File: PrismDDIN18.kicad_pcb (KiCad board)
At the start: 2 copper layers, 280 x 60 mm, 93 parts, among them CON1 BARREL_JACK, IC1 LM2596T-5, J1 Conn_01x03, M1 IN-18, M10 IN-18, Q2 2N7000, Q3 2N7000, Q4 2N7000, Q5 2N7000, Q6 IRF540N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

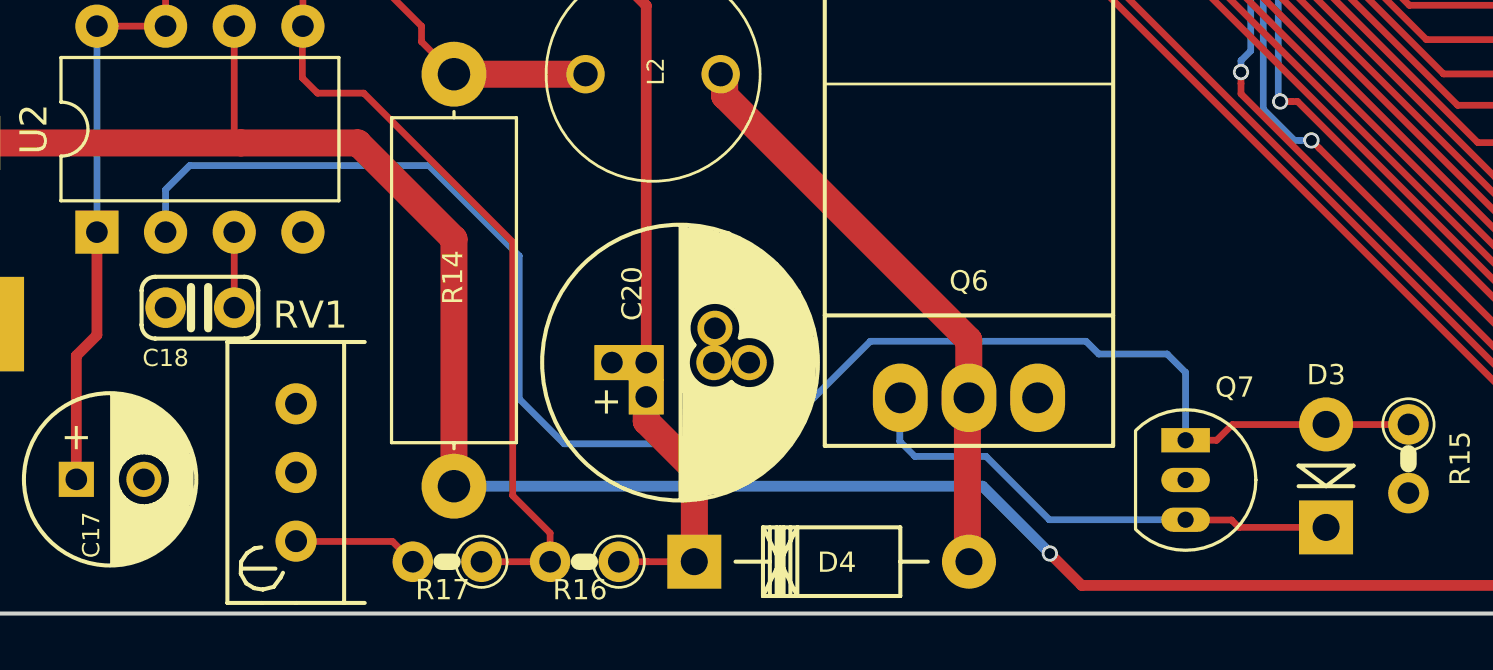
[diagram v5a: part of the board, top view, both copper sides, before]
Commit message: Correct 2N3906 pin out
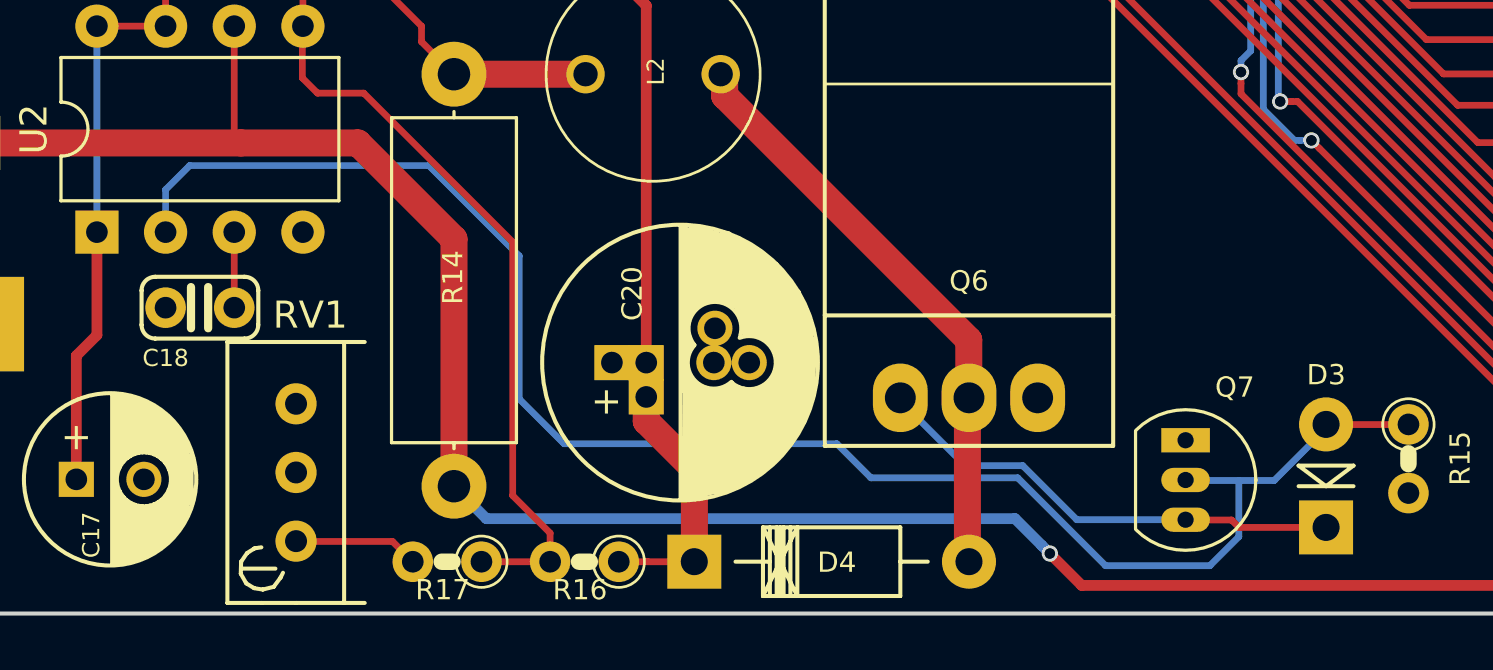
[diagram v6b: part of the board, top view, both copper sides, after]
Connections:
- Q7 pad 1: Net-(D3-Pad2) -> GND
- Q7 pad 2: GND -> Net-(D3-Pad2)
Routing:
- net Net-(D3-Pad2): track 60.1 -> 62.6 mm
- net Net-(D3-Pad1): track 18.8 -> 17.9 mm
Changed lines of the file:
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@@
     (thickness 1.6)
     (drawings 17)
-    (tracks 1350)
+    (tracks 1351)
     (zones 0)
     (modules 93)
@@
     )
     (pad 1 thru_hole rect (at -0.2 0 90) (size 0.9 1.8) (drill 0.6) (layers *.Cu *.Mask)
-      (net 115 "Net-(D3-Pad2)"))
+      (net 7 GND))
     (pad 3 thru_hole oval (at 2.74 0 90) (size 0.9 1.8) (drill 0.6) (layers *.Cu *.Mask)
       (net 114 "Net-(D3-Pad1)"))
     (pad 2 thru_hole oval (at 1.27 0 90) (size 0.9 1.8) (drill 0.6) (layers *.Cu *.Mask)
-      (net 7 GND))
+      (net 115 "Net-(D3-Pad2)"))
     (model ${KISYS3DMOD}/TO_SOT_Packages_THT.3dshapes/TO-92_Inline_Narrow_Oval.wrl
       (offset (xyz 1.269999980926514 0 0))
@@
   (segment (start 301.19 164.47) (end 305.35 160.31) (width 0.25) (layer F.Cu) (net 14) (status 20))
   (via (at 144.47 163.78) (size 0.6) (drill 0.4) (layers F.Cu B.Cu) (net 14))
-  (segment (start 141.98 161.29) (end 144.47 163.78) (width 0.4) (layer B.Cu) (net 14))
-  (segment (start 122.428 161.29) (end 141.98 161.29) (width 0.4) (layer B.Cu) (net 14) (status 10))
   (segment (start 291.62 164.96) (end 293.78 162.8) (width 0.4) (layer F.Cu) (net 14))
   (segment (start 144.47 163.78) (end 145.65 164.96) (width 0.4) (layer F.Cu) (net 14))
   (segment (start 145.65 164.96) (end 291.62 164.96) (width 0.4) (layer F.Cu) (net 14))
+  (segment (start 123.627999 162.489999) (end 143.179999 162.489999) (width 0.4) (layer B.Cu) (net 14))
+  (segment (start 122.428 161.29) (end 123.627999 162.489999) (width 0.4) (layer B.Cu) (net 14))
+  (segment (start 144.170001 163.480001) (end 144.47 163.78) (width 0.4) (layer B.Cu) (net 14))
+  (segment (start 143.179999 162.489999) (end 144.170001 163.480001) (width 0.4) (layer B.Cu) (net 14))
   (segment (start 94.488 150.006032) (end 96.881968 152.4) (width 1) (layer F.Cu) (net 15))
   (segment (start 94.488 148.59254) (end 94.488 150.006032) (width 1) (layer F.Cu) (net 15) (status 10))
@@
   (segment (start 151.19 162.54) (end 149.53 162.54) (width 0.25) (layer F.Cu) (net 114) (status 20))
   (segment (start 149.49 162.53) (end 149.28 162.53) (width 0.25) (layer B.Cu) (net 114) (status 30))
-  (segment (start 138.92 159.63) (end 138.92 158.11) (width 0.25) (layer B.Cu) (net 114))
-  (segment (start 139.48 160.19) (end 138.92 159.63) (width 0.25) (layer B.Cu) (net 114))
-  (segment (start 142.11 160.19) (end 139.48 160.19) (width 0.25) (layer B.Cu) (net 114))
-  (segment (start 149.49 162.53) (end 144.45 162.53) (width 0.25) (layer B.Cu) (net 114))
-  (segment (start 144.45 162.53) (end 142.11 160.19) (width 0.25) (layer B.Cu) (net 114))
-  (segment (start 150.64 159.59) (end 151.22 159.01) (width 0.25) (layer F.Cu) (net 115))
-  (segment (start 149.49 159.59) (end 150.64 159.59) (width 0.25) (layer F.Cu) (net 115) (status 10))
-  (segment (start 151.22 159.01) (end 154.66 159.01) (width 0.25) (layer F.Cu) (net 115) (status 20))
+  (segment (start 149.49 162.53) (end 145.46641 162.53) (width 0.25) (layer B.Cu) (net 114))
+  (segment (start 141.339989 160.529989) (end 138.92 158.11) (width 0.25) (layer B.Cu) (net 114))
+  (segment (start 145.46641 162.53) (end 143.4664 160.529989) (width 0.25) (layer B.Cu) (net 114))
+  (segment (start 143.4664 160.529989) (end 141.339989 160.529989) (width 0.25) (layer B.Cu) (net 114))
   (segment (start 154.66 159.01) (end 157.78 159.01) (width 0.25) (layer F.Cu) (net 115) (status 30))
-  (segment (start 111.76 150.32) (end 111.76 151.892) (width 0.25) (layer B.Cu) (net 115))
-  (segment (start 121.5 149.43) (end 112.65 149.43) (width 0.25) (layer B.Cu) (net 115))
-  (segment (start 112.65 149.43) (end 111.76 150.32) (width 0.25) (layer B.Cu) (net 115))
-  (segment (start 124.84 158.06) (end 124.84 152.77) (width 0.25) (layer B.Cu) (net 115))
-  (segment (start 126.5 159.72) (end 124.84 158.06) (width 0.25) (layer B.Cu) (net 115))
-  (segment (start 124.84 152.77) (end 121.5 149.43) (width 0.25) (layer B.Cu) (net 115))
-  (segment (start 134.04 159.72) (end 126.5 159.72) (width 0.25) (layer B.Cu) (net 115))
-  (segment (start 149.49 157.08) (end 148.81 156.4) (width 0.25) (layer B.Cu) (net 115))
-  (segment (start 149.49 159.59) (end 149.49 157.08) (width 0.25) (layer B.Cu) (net 115))
-  (segment (start 146.28 156.4) (end 145.81 155.93) (width 0.25) (layer B.Cu) (net 115))
-  (segment (start 137.83 155.93) (end 134.04 159.72) (width 0.25) (layer B.Cu) (net 115))
-  (segment (start 148.81 156.4) (end 146.28 156.4) (width 0.25) (layer B.Cu) (net 115))
-  (segment (start 145.81 155.93) (end 137.83 155.93) (width 0.25) (layer B.Cu) (net 115))
+  (segment (start 154.75 159.1) (end 152.77 161.08) (width 0.25) (layer B.Cu) (net 115))
+  (segment (start 143.28 160.98) (end 146.53 164.23) (width 0.25) (layer B.Cu) (net 115))
+  (segment (start 150.39 164.23) (end 151.46 163.16) (width 0.25) (layer B.Cu) (net 115))
+  (segment (start 137.85 160.98) (end 143.28 160.98) (width 0.25) (layer B.Cu) (net 115))
+  (segment (start 136.59 159.72) (end 137.85 160.98) (width 0.25) (layer B.Cu) (net 115))
+  (segment (start 126.5 159.72) (end 136.59 159.72) (width 0.25) (layer B.Cu) (net 115))
+  (segment (start 124.84 152.77) (end 124.84 158.06) (width 0.25) (layer B.Cu) (net 115))
+  (segment (start 152.77 161.08) (end 151.46 161.08) (width 0.25) (layer B.Cu) (net 115))
+  (segment (start 124.84 158.06) (end 126.5 159.72) (width 0.25) (layer B.Cu) (net 115))
+  (segment (start 112.65 149.43) (end 121.5 149.43) (width 0.25) (layer B.Cu) (net 115))
+  (segment (start 111.76 151.892) (end 111.76 150.32) (width 0.25) (layer B.Cu) (net 115))
+  (segment (start 151.46 163.16) (end 151.46 161.08) (width 0.25) (layer B.Cu) (net 115))
+  (segment (start 146.53 164.23) (end 150.39 164.23) (width 0.25) (layer B.Cu) (net 115))
+  (segment (start 151.46 161.08) (end 149.46 161.08) (width 0.25) (layer B.Cu) (net 115))
+  (segment (start 111.76 150.32) (end 112.65 149.43) (width 0.25) (layer B.Cu) (net 115))
+  (segment (start 121.5 149.43) (end 124.84 152.77) (width 0.25) (layer B.Cu) (net 115))
   (segment (start 343.175 121.35) (end 342.75 121.35) (width 0.25) (layer F.Cu) (net 116) (status 30))
   (segment (start 344.125 122.3) (end 343.175 121.35) (width 0.25) (layer F.Cu) (net 116) (status 20))
